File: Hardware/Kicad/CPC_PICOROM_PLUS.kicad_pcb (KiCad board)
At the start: 2 copper layers, 89.9 x 61 mm, 9 parts, among them J1 Amstrad_CPC_Plus_Expansion, SW1 Pico Reset, SW2 CPC Reset, U1 Pico

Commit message: Minor updates to PCB
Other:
- board text added: "Original design by Matt Callow May 2023 https://github.com/mattcallow/CPC_PICOROM CPC+ design by Brett Hallen Nov 2024 https://www.youtube.com/@brfff"

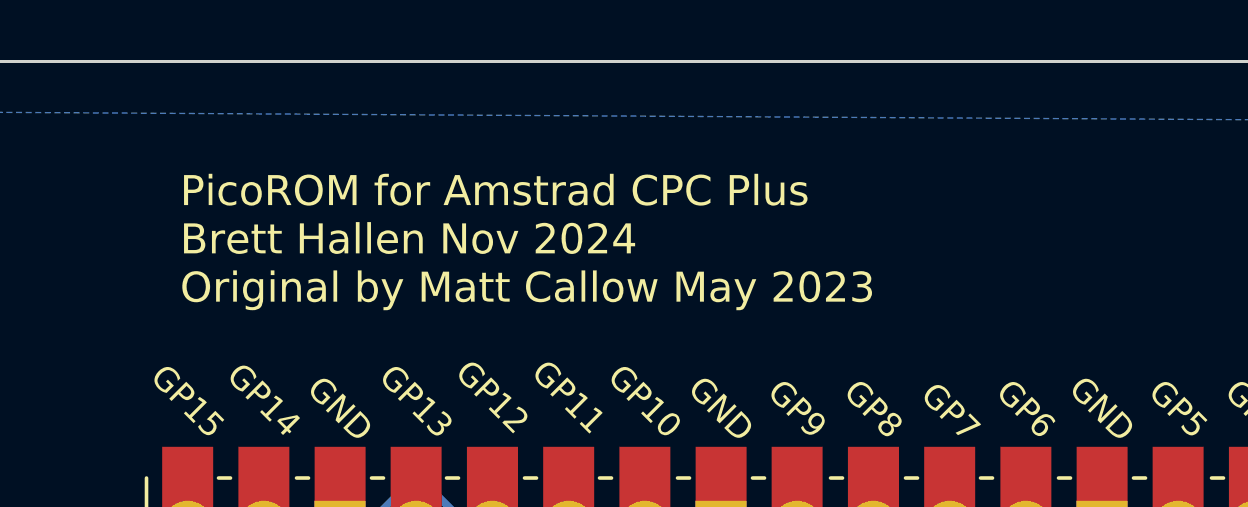
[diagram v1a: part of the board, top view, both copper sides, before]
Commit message: PCB text updates
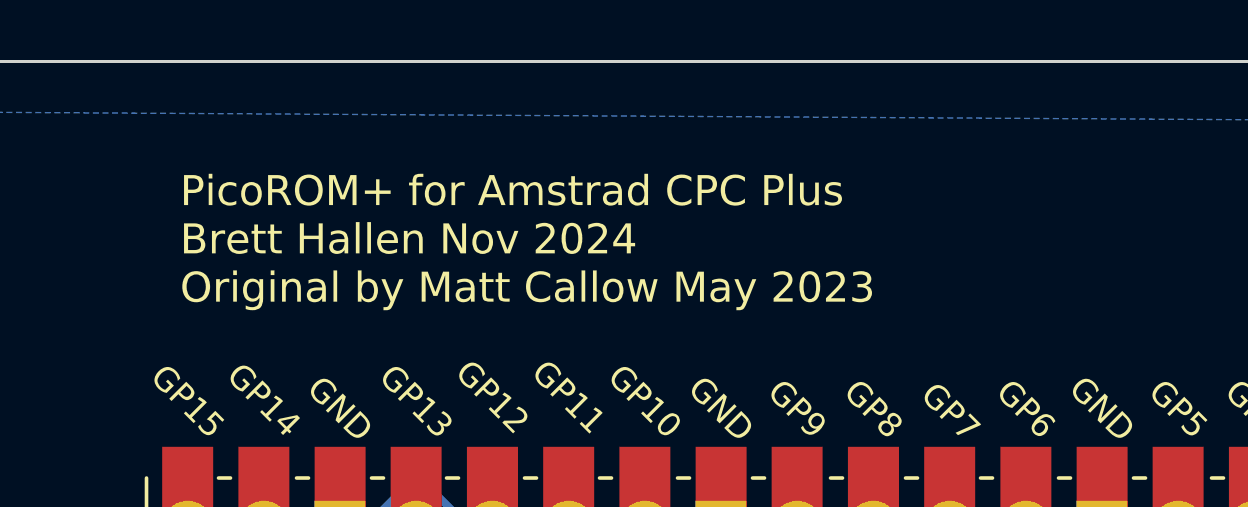
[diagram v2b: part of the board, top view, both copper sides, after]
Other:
- board text added: "PicoROM+ for Amstrad CPC Plus Brett Hallen Nov 2024 Original by Matt Callow May 2023"
- board text removed: "PicoROM for Amstrad CPC Plus Brett Hallen Nov 2024 Original by Matt Callow May 2023"

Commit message: 13-Dec-2024 updates
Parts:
- added JP1: Disable Internal ROMs, Jumper:SolderJumper-2_P1.3mm_Open_RoundedPad1.0x1.5mm, B.Cu at (85.5, 116.6)
- J1: footprint CluelessEngineer:111050113L001 -> Clueless_Engineer:111050113L001_Amstrad_Plus
- SW1, SW2: footprint My_Components:Switch_Tactile_6mm -> Clueless_Engineer:Switch_Tactile_6mm
- U1: footprint CluelessEngineer:RPi_Pico_SMD_TH -> Clueless_Engineer:RPi_Pico_SMD_TH
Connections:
- J1 pad 43: Vcc -> ROMDIS
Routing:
- net Net-(D1-K): track 100.5 -> 0.00 mm
- net ~{BRST}: track 79.4 -> 0.00 mm
- net RUN: track 75.7 -> 0.00 mm
- net Net-(D2-K): track 63.8 -> 0.00 mm
- net /A3: track 59.8 -> 0.00 mm
- net /D1: track 58.0 -> 0.00 mm
- net /A1: track 58.0 -> 0.00 mm
- net Vcc: track 57.8 -> 0.00 mm
- net /A2: track 55.5 -> 0.00 mm
- net /A15: track 55.0 -> 0.00 mm
- net Net-(D3-K): track 55.0 -> 0.00 mm
- net /A0: track 51.7 -> 0.00 mm
- net /D0: track 45.5 -> 0.00 mm, vias 1 -> 0
- net /A12: track 44.4 -> 0.00 mm
- net /D5: track 44.1 -> 0.00 mm
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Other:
- board text added: "1"
- board text added: "2"
- board text added: "49"
- board text added: "50"
- board text added: "A0"
- board text added: "A1"
- board text added: "A10"
- board text added: "A11"
- board text added: "A12"
- board text added: "A13"
- board text added: "A15"
- board text added: "A2"
- board text added: "A3"
- board text added: "A4"
- board text added: "A5"
- board text added: "A6"
- board text added: "A7"
- board text added: "A8"
- board text added: "A9"
- board text added: "D0"
- board text added: "D1"
- board text added: "D2"
- board text added: "D3"
- board text added: "D4"
- board text added: "D5"
- board text added: "D6"
- board text added: "D7"
- board text added: "GND"
- board text added: "ROMDIS"
- board text added: "Vcc"
- board text added: "~{BRST}"
- board text added: "~{IORQ}"
- board text added: "~{ROMEN}"
- board text added: "~{WR}"

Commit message: 13-Dec-2024 update
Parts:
- moved D2 16.3 mm to (99.3, 114.0), turned to 180 degrees
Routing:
- net ~{BRST}: track 0.00 -> 87.2 mm, vias 0 -> 1
- net RUN: track 0.00 -> 81.8 mm, vias 0 -> 1
- net /A0: track 0.00 -> 81.2 mm, vias 0 -> 1
- net Net-(D1-K): track 0.00 -> 80.3 mm
- net /A2: track 0.00 -> 79.5 mm, vias 0 -> 1
- net /A1: track 0.00 -> 76.8 mm, vias 0 -> 1
- net /A4: track 0.00 -> 73.7 mm, vias 0 -> 1
- net /A6: track 0.00 -> 73.7 mm, vias 0 -> 1
- net /A3: track 0.00 -> 72.0 mm, vias 0 -> 1
- net /A8: track 0.00 -> 70.8 mm, vias 0 -> 1
- net /A5: track 0.00 -> 70.0 mm, vias 0 -> 1
- net /A7: track 0.00 -> 67.9 mm, vias 0 -> 1
- net Vcc: track 0.00 -> 65.1 mm
- net ROMDIS: track 0.00 -> 62.8 mm, vias 0 -> 1
- net /A12: track 0.00 -> 62.3 mm, vias 0 -> 1
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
